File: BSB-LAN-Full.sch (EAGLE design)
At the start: 119 parts, among them IC1 LAN8710A-EZC, IC2 TPS2375D, IC3 TX4138, IC4 SY8089AAAC, IC6 CH340X, Q1 BC847, Q2 BC857, Q3 BC847, Q4 WPM2015-3/TR, Q5 BC847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

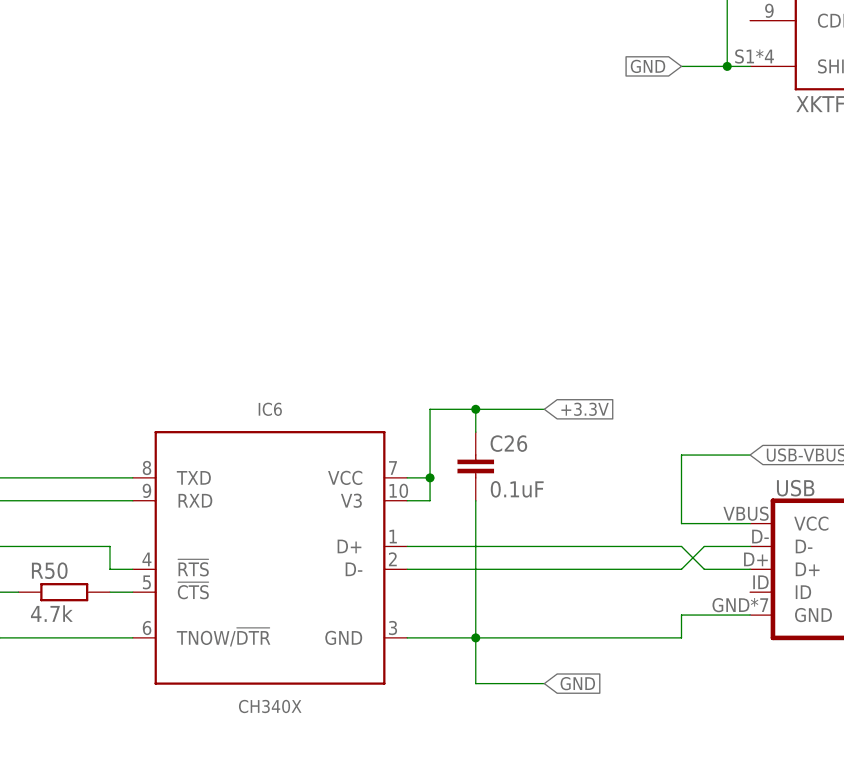
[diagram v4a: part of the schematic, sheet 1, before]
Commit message: Assign JLC Part Numbers
Minor adaptions to available passive parts and packages and now all parts are available in JLCs inventory. LCSC_PART attributes have been applied to aid in BoM creation.

Additionally add extra ESD protection for USB port.
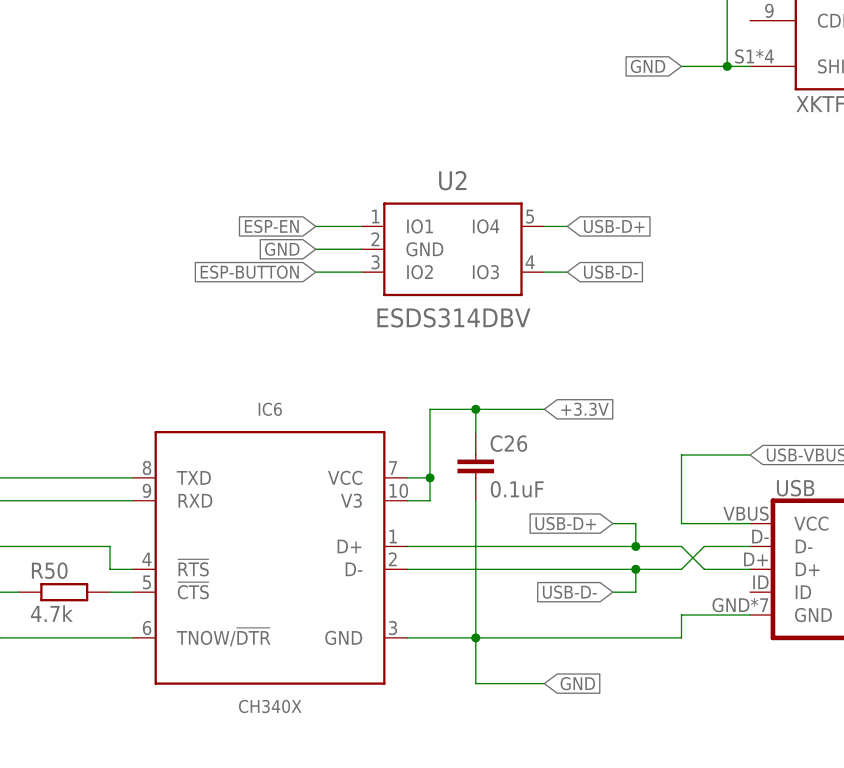
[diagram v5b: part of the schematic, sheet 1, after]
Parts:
- added U2: ESDS314DBV, BSB-LAN:ESDS314DBV
- ACT, PGD: LCSC_PART (none) -> C2286
- C1, C7: LCSC_PART (none) -> C23630
- C10, C11, C12, C17, C26, C27, C3, C8, C9: LCSC_PART (none) -> C1525
- C14: value 15uF 100V -> 22uF 100V; device BSB-LAN:CPOL-EUSMCD -> BSB-LAN:CPOL-EUD; LCSC_PART (none) -> C487431
- C15, C16, C23, C4, C5, C6: LCSC_PART (none) -> C59461
- C18: LCSC_PART (none) -> C4944894
- C19: LCSC_PART (none) -> C1547
- C2, C20, C21: LCSC_PART (none) -> C577300
- C22, C24, C25: device BSB-LAN:C-EUC0603 -> BSB-LAN:C-EUC0805; LCSC_PART (none) -> C45783
- D4: LCSC_PART (none) -> C151246
- D5: LCSC_PART (none) -> C223993
- IC3: LCSC_PART (none) -> C329267
- L1, L2: LCSC_PART (none) -> C1017
- R1, R4, R7: LCSC_PART (none) -> C23137
- R10, R33, R9: LCSC_PART (none) -> C22859
- R11, R13, R14, R19, R28, R32, R34, R47, R51: LCSC_PART (none) -> C25744
- R12, R45, R46: LCSC_PART (none) -> C11702
- R15, R16, R17, R18: LCSC_PART (none) -> C25120
- R2, R48: LCSC_PART (none) -> C22843
- R20, R23, R36, R38, R41, R43: LCSC_PART (none) -> C25852
- R21: LCSC_PART (none) -> C163046
- R24, R26, R40: LCSC_PART (none) -> C25760
- R25, R42, R44: LCSC_PART (none) -> C26972
- R27, R37: LCSC_PART (none) -> C52269
- R29, R3, R30, R31, R35, R49: LCSC_PART (none) -> C25091
- R39: value 4.7R -> 10R; device BSB-LAN:R-EU_R0402 -> BSB-LAN:R-EU_R0603L; LCSC_PART (none) -> C22859
- R5, R50, R6, R8: LCSC_PART (none) -> C25900
- RN1, RN2, RN3: LCSC_PART (none) -> C414564
- U$3: value OSHW-LOGOM -> DNI
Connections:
- net ESP-BUTTON: now also U2.IO2
- net ESP-EN: now also U2.IO1
- net GND: now also U2.GND
- net USB-D+: now also U2.IO4
- net USB-D-: now also U2.IO3

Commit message: Begin optimising for assembly cost
Trying to reduce the number of different components, as well as instances where the same component is used on two sides of the board (incurs double assembly setup fee).
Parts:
- C10, C11, C17, C26, C27, C8, C9: device BSB-LAN:C-EUC0402 -> BSB-LAN:C-EUC0603L; LCSC_PART C1525 -> C113803
- C12, C3: device BSB-LAN:C-EUC0402 -> BSB-LAN:C-EUC0603; LCSC_PART C1525 -> C113803
- C15, C16, C4, C5, C6: device BSB-LAN:C-EUC0603 -> BSB-LAN:C-EUC0805L; LCSC_PART C59461 -> C45783
- C23: device BSB-LAN:C-EUC0603 -> BSB-LAN:C-EUC0805; LCSC_PART C59461 -> C45783
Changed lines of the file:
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@@
 <attribute name="LCSC_PART" value="C577300"/>
 </part>
-<part name="C3" library="BSB-LAN" deviceset="C-EU" device="C0402" value="0.1uF">
-<attribute name="LCSC_PART" value="C1525"/>
+<part name="C3" library="BSB-LAN" deviceset="C-EU" device="C0603" value="0.1uF">
+<attribute name="LCSC_PART" value="C113803"/>
 </part>
 <part name="RN1" library="BSB-LAN" deviceset="R-NET-04" device="-R1206" value="2.2k">
@@
 <attribute name="LCSC_PART" value="C25744"/>
 </part>
-<part name="C4" library="BSB-LAN" deviceset="C-EU" device="C0603" value="22uF">
-<attribute name="LCSC_PART" value="C59461"/>
-</part>
-<part name="C5" library="BSB-LAN" deviceset="C-EU" device="C0603" value="22uF">
-<attribute name="LCSC_PART" value="C59461"/>
-</part>
-<part name="C6" library="BSB-LAN" deviceset="C-EU" device="C0603" value="22uF">
-<attribute name="LCSC_PART" value="C59461"/>
+<part name="C4" library="BSB-LAN" deviceset="C-EU" device="C0805L" value="22uF">
+<attribute name="LCSC_PART" value="C45783"/>
+</part>
+<part name="C5" library="BSB-LAN" deviceset="C-EU" device="C0805L" value="22uF">
+<attribute name="LCSC_PART" value="C45783"/>
+</part>
+<part name="C6" library="BSB-LAN" deviceset="C-EU" device="C0805L" value="22uF">
+<attribute name="LCSC_PART" value="C45783"/>
 </part>
 <part name="R12" library="BSB-LAN" deviceset="R-EU_" device="R0402" value="1k">
 <attribute name="LCSC_PART" value="C11702"/>
 </part>
-<part name="C10" library="BSB-LAN" deviceset="C-EU" device="C0402" value="0.1uF">
-<attribute name="LCSC_PART" value="C1525"/>
-</part>
-<part name="C8" library="BSB-LAN" deviceset="C-EU" device="C0402" value="0.1uF">
-<attribute name="LCSC_PART" value="C1525"/>
-</part>
-<part name="C9" library="BSB-LAN" deviceset="C-EU" device="C0402" value="0.1uF">
-<attribute name="LCSC_PART" value="C1525"/>
+<part name="C10" library="BSB-LAN" deviceset="C-EU" device="C0603L" value="0.1uF">
+<attribute name="LCSC_PART" value="C113803"/>
+</part>
+<part name="C8" library="BSB-LAN" deviceset="C-EU" device="C0603L" value="0.1uF">
+<attribute name="LCSC_PART" value="C113803"/>
+</part>
+<part name="C9" library="BSB-LAN" deviceset="C-EU" device="C0603L" value="0.1uF">
+<attribute name="LCSC_PART" value="C113803"/>
 </part>
 <part name="C7" library="BSB-LAN" deviceset="C-EU" device="C0603" value="2.2uF">
 <attribute name="LCSC_PART" value="C23630"/>
 </part>
-<part name="C11" library="BSB-LAN" deviceset="C-EU" device="C0402" value="0.1uF">
-<attribute name="LCSC_PART" value="C1525"/>
+<part name="C11" library="BSB-LAN" deviceset="C-EU" device="C0603L" value="0.1uF">
+<attribute name="LCSC_PART" value="C113803"/>
 </part>
 <part name="R16" library="BSB-LAN" deviceset="R-EU_" device="R0402L" value="49.9R">
@@
 <attribute name="LCSC_PART" value="C25852"/>
 </part>
-<part name="C12" library="BSB-LAN" deviceset="C-EU" device="C0402" value="0.1uF">
-<attribute name="LCSC_PART" value="C1525"/>
+<part name="C12" library="BSB-LAN" deviceset="C-EU" device="C0603" value="0.1uF">
+<attribute name="LCSC_PART" value="C113803"/>
 </part>
 <part name="R23" library="BSB-LAN" deviceset="R-EU_" device="R0402" value="12.1k 1%">
@@
 <attribute name="LCSC_PART" value="C1017"/>
 </part>
-<part name="C15" library="BSB-LAN" deviceset="C-EU" device="C0603" value="22uF">
-<attribute name="LCSC_PART" value="C59461"/>
-</part>
-<part name="C16" library="BSB-LAN" deviceset="C-EU" device="C0603" value="22uF">
-<attribute name="LCSC_PART" value="C59461"/>
+<part name="C15" library="BSB-LAN" deviceset="C-EU" device="C0805L" value="22uF">
+<attribute name="LCSC_PART" value="C45783"/>
+</part>
+<part name="C16" library="BSB-LAN" deviceset="C-EU" device="C0805L" value="22uF">
+<attribute name="LCSC_PART" value="C45783"/>
 </part>
 <part name="RN3" library="BSB-LAN" deviceset="R-NET-04" device="-R1206" value="2.2k">
@@
 <attribute name="LCSC_PART" value="C25091"/>
 </part>
-<part name="C17" library="BSB-LAN" deviceset="C-EU" device="C0402" value="0.1uF">
-<attribute name="LCSC_PART" value="C1525"/>
+<part name="C17" library="BSB-LAN" deviceset="C-EU" device="C0603L" value="0.1uF">
+<attribute name="LCSC_PART" value="C113803"/>
 </part>
 <part name="R21" library="BSB-LAN" deviceset="R-EU_" device="R1206" value="0.03R 1%">
@@
 <attribute name="LCSC_PART" value="C135262"/>
 </part>
-<part name="C23" library="BSB-LAN" deviceset="C-EU" device="C0603" value="22uF">
-<attribute name="LCSC_PART" value="C59461"/>
+<part name="C23" library="BSB-LAN" deviceset="C-EU" device="C0805" value="22uF">
+<attribute name="LCSC_PART" value="C45783"/>
 </part>
 <part name="C24" library="BSB-LAN" deviceset="C-EU" device="C0805" value="22uF">
@@
 <attribute name="LCSC_PART" value="C2286"/>
 </part>
-<part name="C26" library="BSB-LAN" deviceset="C-EU" device="C0402" value="0.1uF">
-<attribute name="LCSC_PART" value="C1525"/>
+<part name="C26" library="BSB-LAN" deviceset="C-EU" device="C0603L" value="0.1uF">
+<attribute name="LCSC_PART" value="C113803"/>
 </part>
 <part name="R50" library="BSB-LAN" deviceset="R-EU_" device="R0402" value="4.7k">
@@
 </part>
 <part name="USB" library="BSB-LAN" deviceset="USB_MICROB_PLUG" device="" value="ZX62-B-5PA(33)"/>
-<part name="C27" library="BSB-LAN" deviceset="C-EU" device="C0402" value="0.1uF">
-<attribute name="LCSC_PART" value="C1525"/>
+<part name="C27" library="BSB-LAN" deviceset="C-EU" device="C0603L" value="0.1uF">
+<attribute name="LCSC_PART" value="C113803"/>
 </part>
 <part name="CASE1" library="BSB-LAN" deviceset="CNMB" device="/2" value="DNI"/>

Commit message: Move LAN IC to Top Side
With LAN IC on the top side, the board could be manufactered with only the top-side components populated, and with the exception of the uSD card all the bottom side parts are then relatively easy to hand solder with care.
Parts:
- C12: device BSB-LAN:C-EUC0603 -> BSB-LAN:C-EUC0603L
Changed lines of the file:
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@@
 <attribute name="LCSC_PART" value="C25852"/>
 </part>
-<part name="C12" library="BSB-LAN" deviceset="C-EU" device="C0603" value="0.1uF">
+<part name="C12" library="BSB-LAN" deviceset="C-EU" device="C0603L" value="0.1uF">
 <attribute name="LCSC_PART" value="C113803"/>
 </part>
